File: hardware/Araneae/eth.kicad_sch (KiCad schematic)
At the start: 24 parts, among them U6 KSZ9893RNXI, U7 TLV75518PDBV, Y2 25MHz

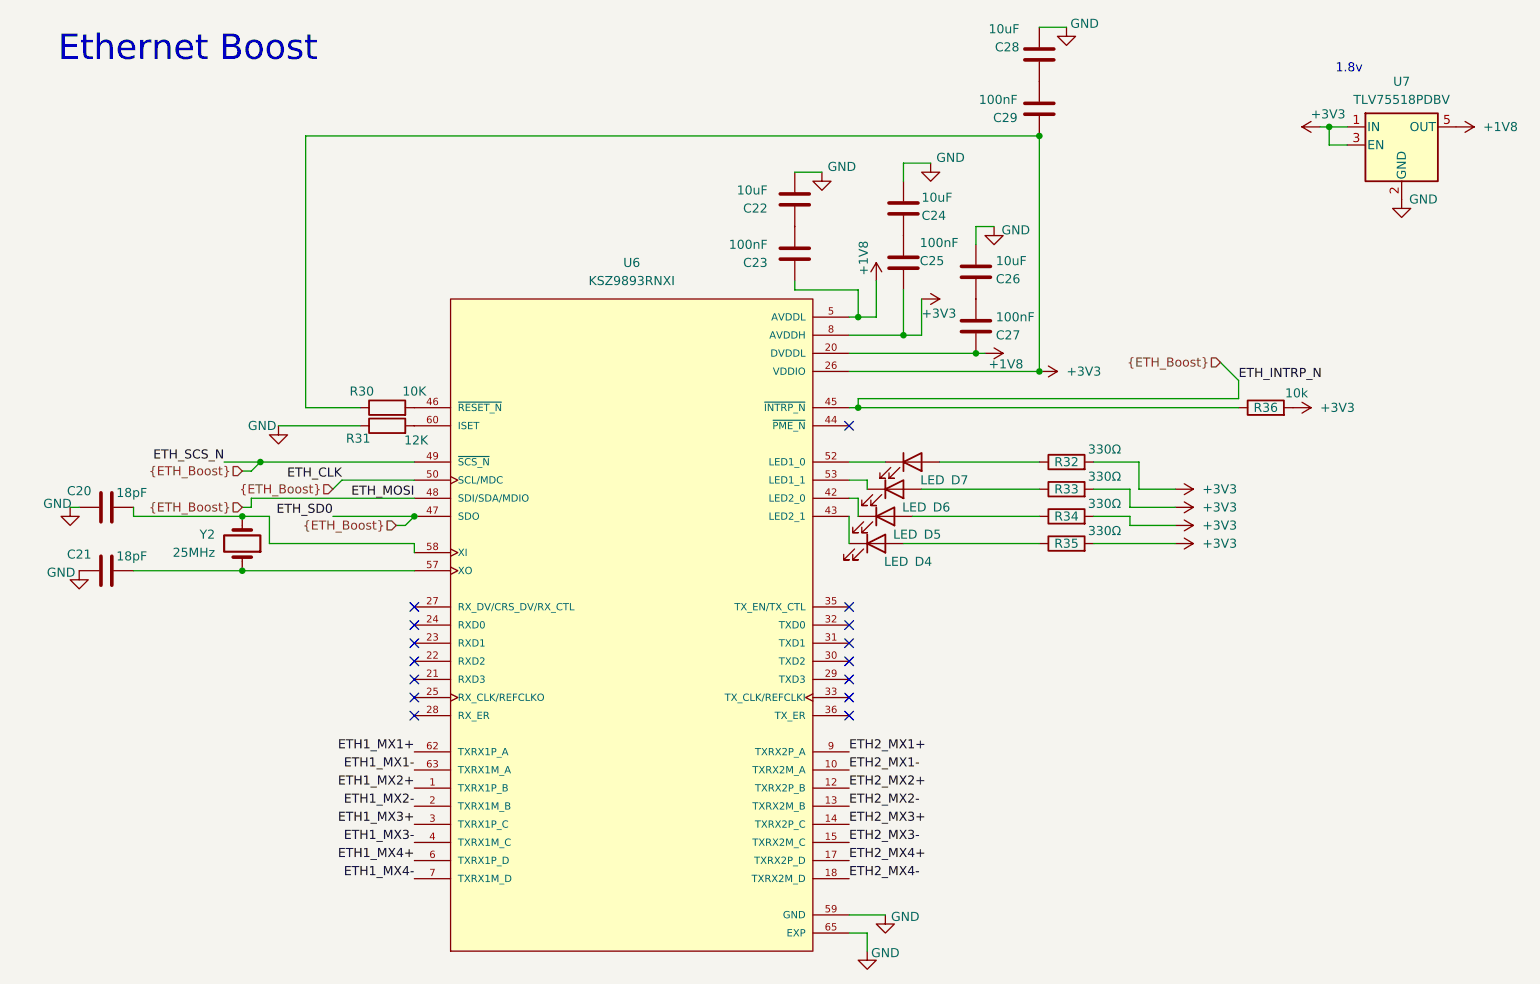
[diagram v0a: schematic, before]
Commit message: Add CI workflow for PCB checks and artifact generation
- Created a GitHub Actions workflow (`ci.yml`) to automate hardware checks including ERC, DRC, and plot generation for KiCad projects.
- Added a new footprint for the SON50P200X200X80-9N component in `SON50P200X200X80-9N.kicad_mod`.
- Introduced a new symbol for the TPS22965DSGR component in `TPS22965DSGR.kicad_sym`.
- Added a configuration file `kibot.yaml` for generating fabrication files and other outputs.
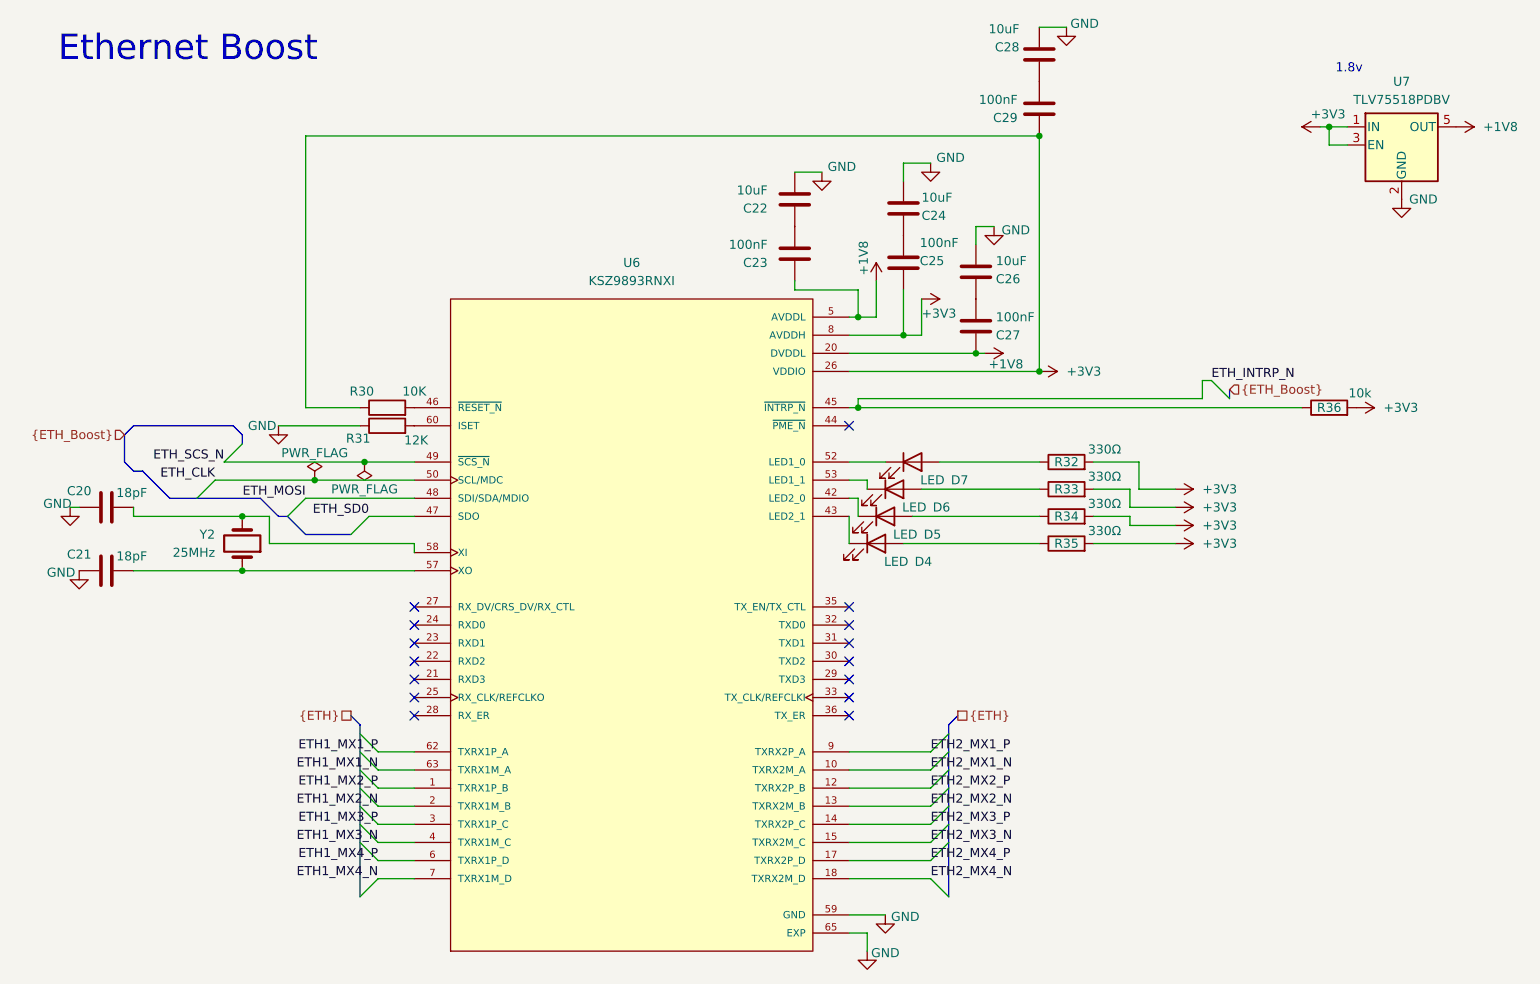
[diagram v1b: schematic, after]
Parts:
- C20, C21, C23, C25, C27, C29: footprint (none) -> Capacitor_SMD:C_0603_1608Metric
- C22, C24, C26, C28: footprint (none) -> Capacitor_SMD:C_0805_2012Metric
- D4, D5, D6, D7: footprint (none) -> LED_SMD:LED_0805_2012Metric
- R30, R31, R32, R33, R34, R35, R36: footprint (none) -> Resistor_SMD:R_0603_1608Metric
- U6: footprint KSZ9893RNXI:QFN40P800X800X90-65N -> OPL:QFN40P800X800X90-65N
- Y2: footprint (none) -> Crystal:Crystal_SMD_3225-4Pin_3.2x2.5mm
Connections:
- net {ETH_Boost}: no longer R36.1, U6.45 (~{INTRP_N}), U6.47 (SDO), U6.48 (SDI/SDA/MDIO), U6.49 (~{SCS_N}), U6.50 (SCL/MDC)
- net ETH1_MX1+ renamed ETH1_MX1_P
- net ETH1_MX1- renamed ETH1_MX1_N
- net ETH1_MX2+ renamed ETH1_MX2_P
- net ETH1_MX2- renamed ETH1_MX2_N
- net ETH1_MX3+ renamed ETH1_MX3_P
- net ETH1_MX3- renamed ETH1_MX3_N
- net ETH1_MX4+ renamed ETH1_MX4_P
- net ETH1_MX4- renamed ETH1_MX4_N
- net ETH2_MX1+ renamed ETH2_MX1_P
- net ETH2_MX1- renamed ETH2_MX1_N
- net ETH2_MX2+ renamed ETH2_MX2_P
- net ETH2_MX2- renamed ETH2_MX2_N
- net ETH2_MX3+ renamed ETH2_MX3_P
- net ETH2_MX3- renamed ETH2_MX3_N
- net ETH2_MX4+ renamed ETH2_MX4_P
- net ETH2_MX4- renamed ETH2_MX4_N
- new net ETH_CLK: U6.50 (SCL/MDC)
- new net ETH_INTRP_N: R36.1, U6.45 (~{INTRP_N})
- new net ETH_MOSI: U6.48 (SDI/SDA/MDIO)
- new net ETH_SCS_N: U6.49 (~{SCS_N})
- new net ETH_SD0: U6.47 (SDO)
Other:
- company: (none) -> Matheus Henrique(Aka: TheusHen)
- title: (none) -> Araneae
- moved on the sheet: R36
